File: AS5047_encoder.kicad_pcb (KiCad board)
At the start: 2 copper layers, 8 parts, among them P1 CONN_01X07, U1 AS5047

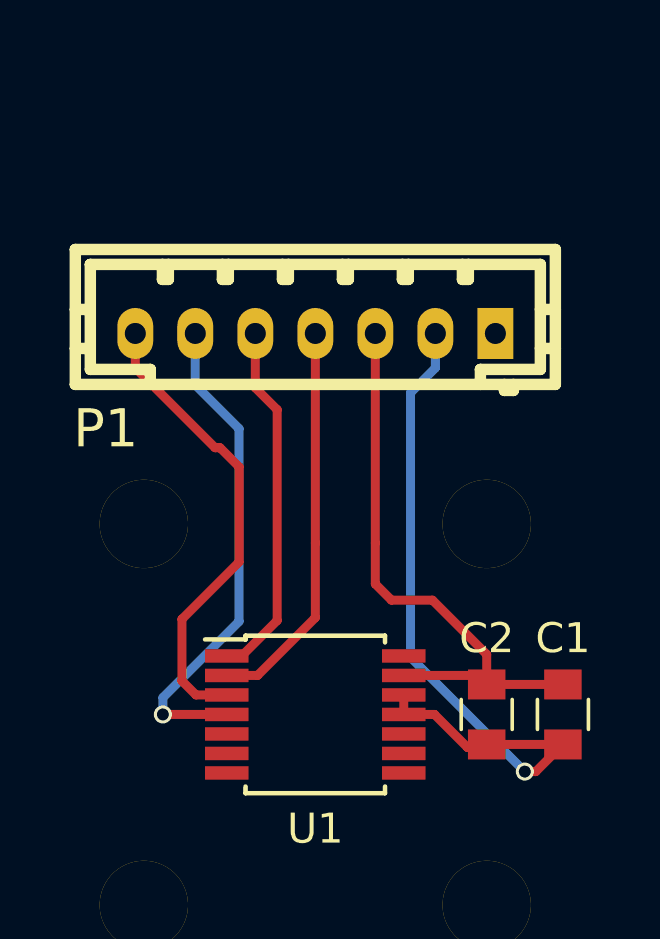
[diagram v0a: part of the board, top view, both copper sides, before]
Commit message: Change connector and update component associations.
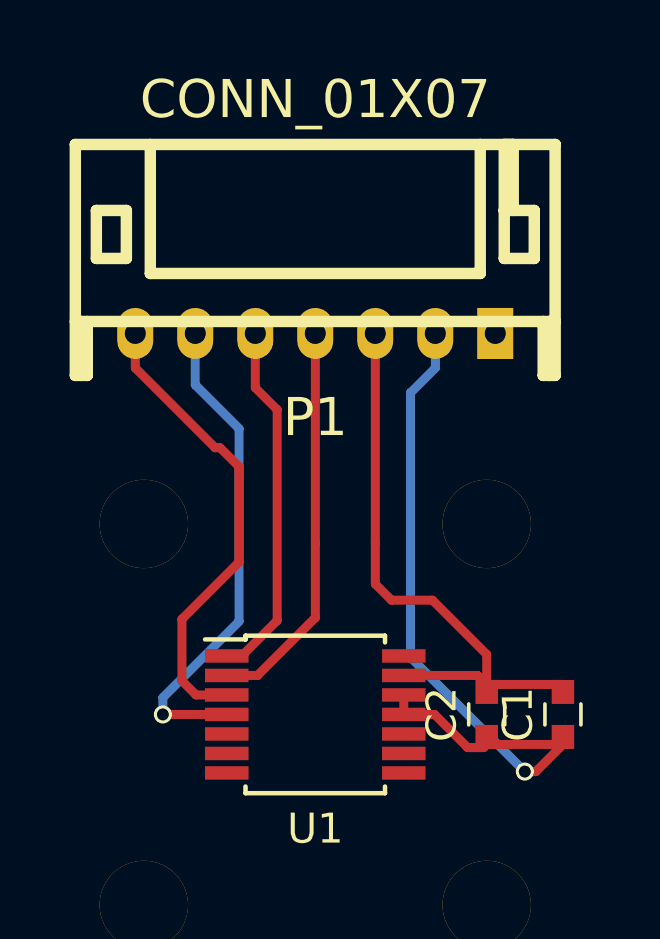
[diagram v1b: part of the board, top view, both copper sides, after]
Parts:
- C1, C2: footprint Capacitors_SMD:C_0805 -> Capacitors_SMD:C_0603
- P1: footprint w_conn_jst-ph:b7b-ph-kl -> w_conn_jst-ph:s7b-ph-kl

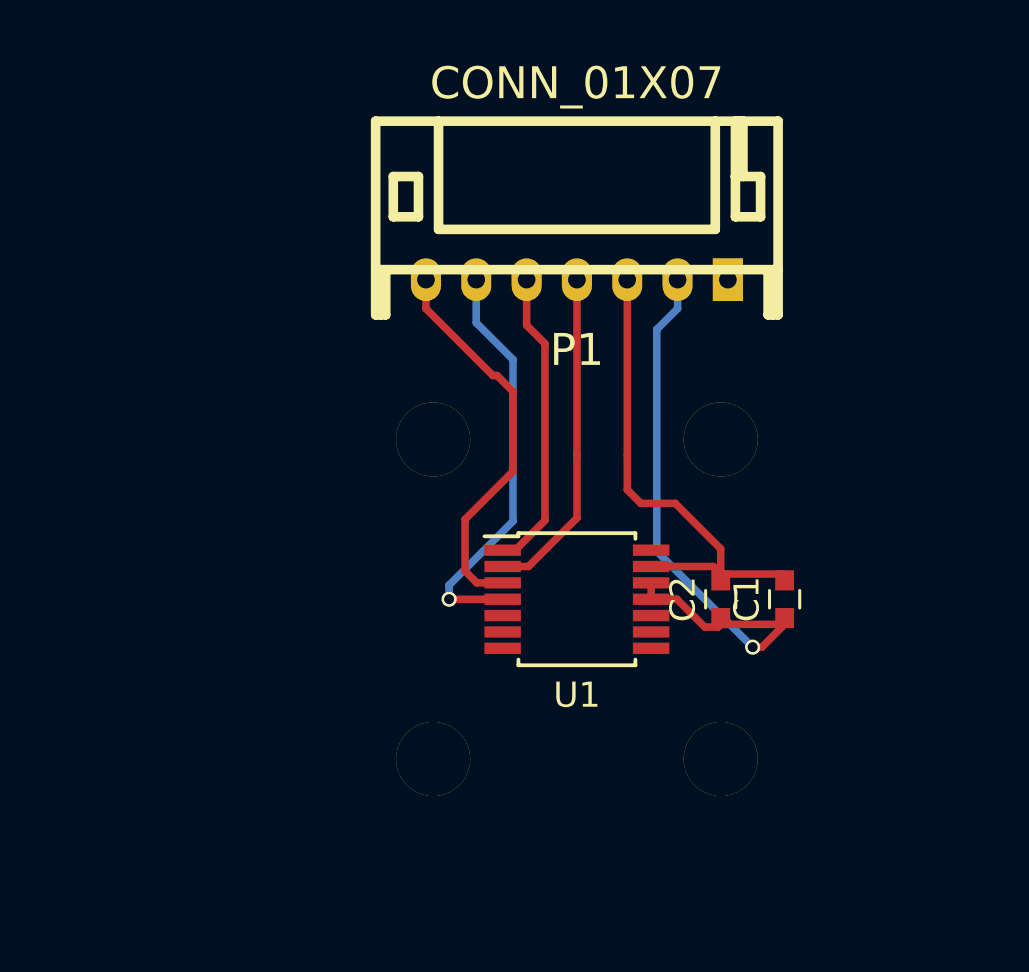
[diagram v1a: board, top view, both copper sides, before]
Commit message: Fixed outline. Generated gerbers. Added BOM. Ordered a batch of boards.
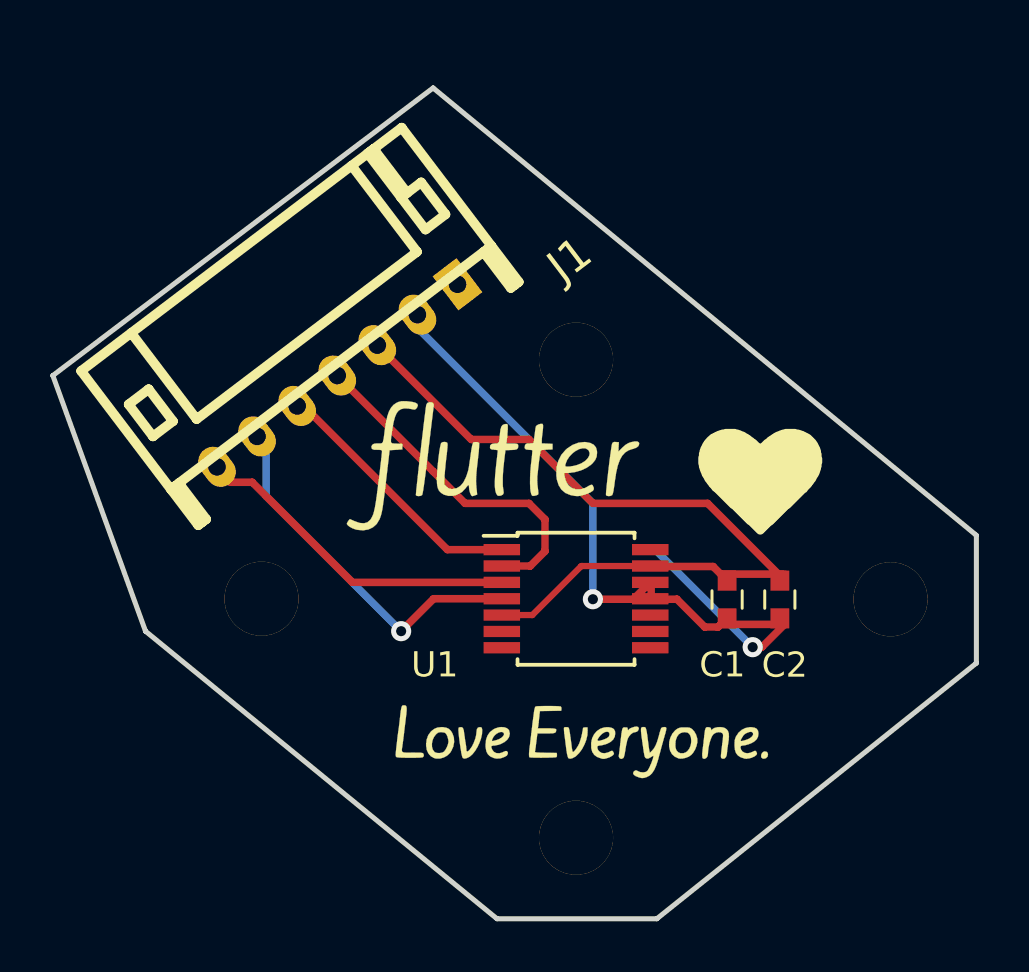
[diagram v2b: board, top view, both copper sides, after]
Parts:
- added G***: LOGO, vesc_encoder:love_small, F.Cu at (89.8, 102.1)
- added G***: LOGO, vesc_encoder:flutter_small, F.Cu at (86.5, 91.2)
- moved REF** 13.7 mm to (88.9, 102.9)
- moved J1 10.3 mm to (80.0, 87.6), turned to 217.2 degrees
- moved REF** 9.92 mm to (102.9, 96.5)
- moved REF** 8.98 mm to (77.5, 96.5)
- moved REF** 6.35 mm to (88.9, 90.2)
- moved C2 2.35 mm to (97.6, 96.5)
- moved C1 2.29 mm to (95.5, 96.5)
- renumbered P1 to J1
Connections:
- net Net-(C1-Pad1) renamed /VCC
- net Net-(P1-Pad4) renamed /CLK
- net Net-(P1-Pad5) renamed /CSn
- net Net-(P1-Pad6) renamed /MOSI
- net Net-(P1-Pad7) renamed /MISO
- U1 pad 5: Net-(U1-Pad5) -> GND
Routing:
- net GND: track 19.5 -> 32.1 mm
- net /VCC: track 24.6 -> 30.7 mm, vias 1 -> 2
- net /MISO: track 15.6 -> 13.5 mm
- net /MOSI: track 16.5 -> 14.8 mm
- net /CSn: track 12.0 -> 10.7 mm
- net /CLK: track 13.2 -> 13.9 mm
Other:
- board outline added: 36.7 x 33 mm
- net class Default: clearance 0.2 -> 0.1524; trace_width 0.3 -> 0.25
- rule trace_clearance: 0.2 -> 0.1524

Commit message: Imported to a new Kicad install and removed remnant traces from PCB layout. Suggest re-export gerbers to remove benign extra trace.
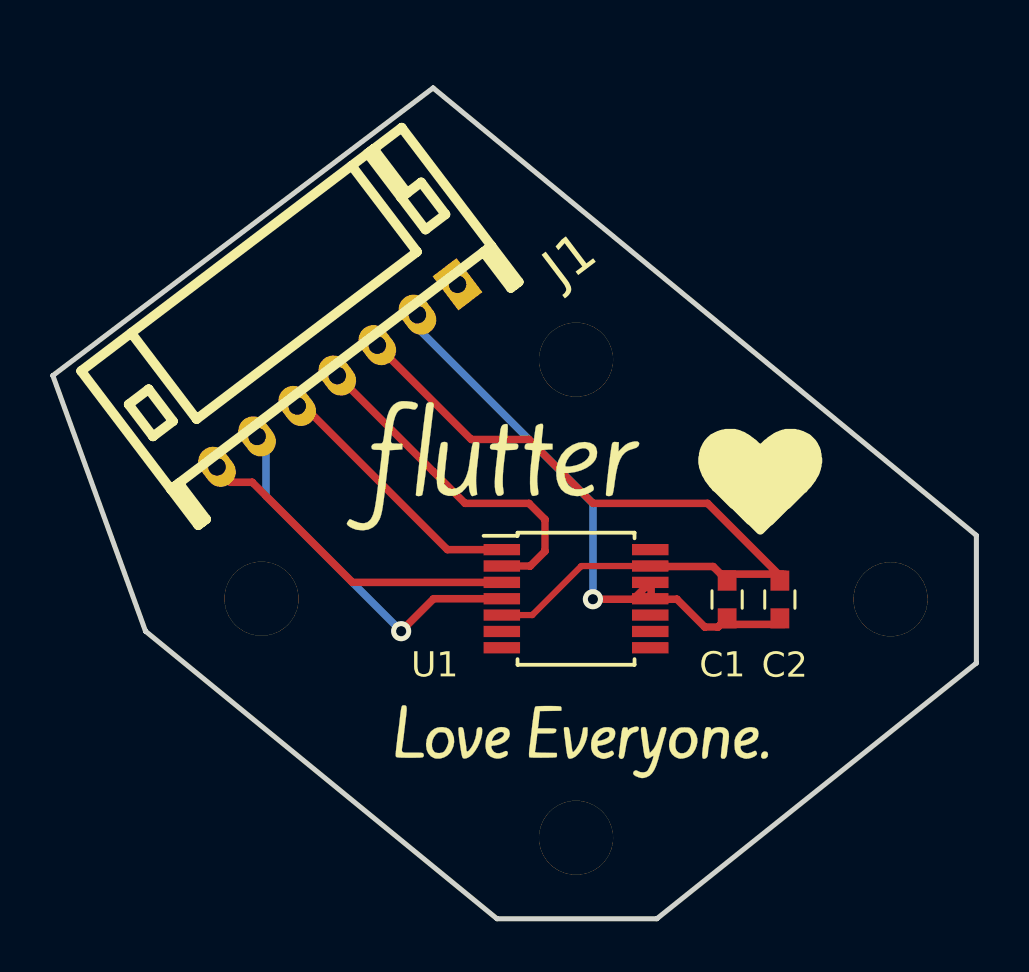
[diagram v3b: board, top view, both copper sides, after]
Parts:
- ? (x4): renamed from REF**; value VAL** -> (none)
- ? (x2): renamed from G***; value LOGO -> (none)
- C1, C2: value C -> (none)
- J1: value CONN_01X07 -> (none)
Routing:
- net /VCC: track 30.7 -> 23.6 mm, vias 2 -> 1
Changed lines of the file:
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@@
-(kicad_pcb (version 4) (host pcbnew 4.0.7+dfsg1-1)
+(kicad_pcb (version 20171130) (host pcbnew 5.0.2+dfsg1-1)
   (general
-    (links 0)
-    (no_connects 0)
-    (area 67.030233 75.194993 105.510001 109.320001)
     (thickness 1.6)
-    (drawings 9)
-    (tracks 52)
+    (drawings 11)
+    (tracks 48)
     (zones 0)
     (modules 10)
@@
     (36 B.SilkS user)
     (37 F.SilkS user)
-    (38 B.Mask user)
+    (38 B.Mask user hide)
     (39 F.Mask user)
-    (40 Dwgs.User user hide)
-    (41 Cmts.User user hide)
+    (40 Dwgs.User user)
+    (41 Cmts.User user)
     (42 Eco1.User user hide)
     (43 Eco2.User user hide)
@@
     (47 F.CrtYd user hide)
     (48 B.Fab user hide)
-    (49 F.Fab user hide)
+    (49 F.Fab user)
   )
   (setup
@@
     (pad_drill 0.762)
     (pad_to_mask_clearance 0.2)
+    (solder_mask_min_width 0.25)
     (aux_axis_origin 0 0)
-    (visible_elements FFFD5FBF)
+    (visible_elements FFFFDFFF)
     (pcbplotparams
       (layerselection 0x010fc_80000001)
       (usegerberextensions true)
+      (usegerberattributes false)
+      (usegerberadvancedattributes false)
+      (creategerberjobfile false)
       (excludeedgelayer true)
       (linewidth 0.100000)
@@
       (hpglpennumber 1)
       (hpglpenspeed 20)
-      (hpglpendiameter 15)
-      (hpglpenoverlay 2)
+      (hpglpendiameter 15.000000)
       (psnegative false)
       (psa4output false)
@@
       (drillshape 0)
       (scaleselection 1)
-      (outputdirectory Gerber))
+      (outputdirectory "Gerber"))
   )
   (net 0 "")
@@
     (descr "JST PH series connector, S7B-PH-KL")
     (fp_text reference J1 (at -10.138672 -1.905389 217.2) (layer F.SilkS)
-      (effects (font (thickness 0.3048)))
-    )
-    (fp_text value CONN_01X07 (at 0.810465 9.225022 217.2) (layer F.SilkS) hide
-      (effects (font (thickness 0.3048)))
+      (effects (font (size 1.524 1.524) (thickness 0.3048)))
+    )
+    (fp_text value "" (at 0.810465 9.225022 217.2) (layer F.SilkS) hide
+      (effects (font (size 1.524 1.524) (thickness 0.3048)))
     )
     (fp_line (start -6.2992 4.09956) (end -6.2992 6.2992) (layer F.SilkS) (width 0.381))
@@
     (pad 2 thru_hole oval (at -4.0005 0 217.2) (size 1.19888 1.69926) (drill 0.70104) (layers *.Cu *.Mask F.SilkS)
       (net 8 /VCC))
-    (pad 3 thru_hole oval (at -1.99898 0 217.2) (size 1.19888 1.69926) (drill 0.70104) (layers *.Cu *.Mask F.SilkS)
+    (pad 3 thru_hole oval (at -1.99898 0.000001 217.2) (size 1.19888 1.69926) (drill 0.70104) (layers *.Cu *.Mask F.SilkS)
       (net 6 GND))
     (pad 4 thru_hole oval (at 0 0 217.2) (size 1.19888 1.69926) (drill 0.70104) (layers *.Cu *.Mask F.SilkS)
       (net 9 /CLK))
-    (pad 5 thru_hole oval (at 1.99898 0 217.2) (size 1.19888 1.69926) (drill 0.70104) (layers *.Cu *.Mask F.SilkS)
+    (pad 5 thru_hole oval (at 1.99898 -0.000001 217.2) (size 1.19888 1.69926) (drill 0.70104) (layers *.Cu *.Mask F.SilkS)
       (net 10 /CSn))
     (pad 6 thru_hole oval (at 4.0005 0 217.2) (size 1.19888 1.69926) (drill 0.70104) (layers *.Cu *.Mask F.SilkS)
@@
     (descr "Mounting Hole - Screw #4")
     (attr virtual)
-    (fp_text reference REF** (at 0 -4.6) (layer F.SilkS) hide
+    (fp_text reference "" (at 0 -2.54) (layer F.SilkS) hide
       (effects (font (size 1 1) (thickness 0.18)))
     )
-    (fp_text value VAL** (at 0 4.7) (layer F.Fab) hide
+    (fp_text value "" (at 0 4.7) (layer F.Fab) hide
       (effects (font (size 1 1) (thickness 0.18)))
     )
@@
     (descr "Mounting Hole - Screw #4")
     (attr virtual)
-    (fp_text reference REF** (at 0 -4.6) (layer F.SilkS) hide
+    (fp_text reference "" (at 0 -4.6) (layer F.SilkS) hide
       (effects (font (size 1 1) (thickness 0.18)))
     )
-    (fp_text value VAL** (at 0 4.7) (layer F.Fab) hide
+    (fp_text value "" (at 0 4.7) (layer F.Fab) hide
       (effects (font (size 1 1) (thickness 0.18)))
     )
@@
     (descr "Mounting Hole - Screw #4")
     (attr virtual)
-    (fp_text reference REF** (at 0 -4.6) (layer F.SilkS) hide
+    (fp_text reference "" (at 0 -4.6) (layer F.SilkS) hide
       (effects (font (size 1 1) (thickness 0.18)))
     )
-    (fp_text value VAL** (at 0 4.7) (layer F.Fab) hide
+    (fp_text value "" (at 0 4.7) (layer F.Fab) hide
       (effects (font (size 1 1) (thickness 0.18)))
     )
@@
     (descr "Mounting Hole - Screw #4")
     (attr virtual)
-    (fp_text reference REF** (at 0 -4.6) (layer F.SilkS) hide
+    (fp_text reference "" (at 0 -4.6) (layer F.SilkS) hide
       (effects (font (size 1 1) (thickness 0.18)))
     )
-    (fp_text value VAL** (at 0 4.7) (layer F.Fab) hide
+    (fp_text value "" (at 0 4.7) (layer F.Fab) hide
       (effects (font (size 1 1) (thickness 0.18)))
     )
@@
       (effects (font (size 1 1) (thickness 0.15)))
     )
-    (fp_text value C (at 0 1.5 90) (layer F.Fab)
+    (fp_text value "" (at 0 1.5 90) (layer F.Fab) hide
       (effects (font (size 1 1) (thickness 0.15)))
     )
@@
       (effects (font (size 1 1) (thickness 0.15)))
     )
-    (fp_text value C (at 0 1.5 90) (layer F.Fab)
+    (fp_text value "" (at 0 1.5 90) (layer F.Fab)
       (effects (font (size 1 1) (thickness 0.15)))
     )
@@
   (module vesc_encoder:love_small (layer Top)
     (at 89.789 102.108)
-    (fp_text reference G*** (at 0 0) (layer F.SilkS) hide
-      (effects (font (thickness 0.3)))
-    )
-    (fp_text value LOGO (at 0.75 0) (layer F.SilkS) hide
-      (effects (font (thickness 0.3)))
+    (fp_text reference "" (at 15.621 5.842) (layer F.SilkS) hide
+      (effects (font (size 1.524 1.524) (thickness 0.3)))
+    )
+    (fp_text value "" (at 0.75 0) (layer F.SilkS) hide
+      (effects (font (size 1.524 1.524) (thickness 0.3)))
     )
     (fp_poly (pts (xy 2.41751 -0.507735) (xy 2.444613 -0.503325) (xy 2.466564 -0.489352) (xy 2.484926 -0.460398)
@@
   (module vesc_encoder:flutter_small (layer Top)
     (at 86.487 91.186)
-    (fp_text reference G*** (at 0 0) (layer F.SilkS) hide
-      (effects (font (thickness 0.3)))
-    )
-    (fp_text value LOGO (at 0.75 0) (layer F.SilkS) hide
-      (effects (font (thickness 0.3)))
+    (fp_text reference "" (at 0 0) (layer F.SilkS) hide
+      (effects (font (size 1.524 1.524) (thickness 0.3)))
+    )
+    (fp_text value "" (at 0.75 0) (layer F.SilkS) hide
+      (effects (font (size 1.524 1.524) (thickness 0.3)))
     )
     (fp_poly (pts (xy -3.708083 -2.532209) (xy -3.703806 -2.531935) (xy -3.506396 -2.510907) (xy -3.369681 -2.476387)
@@
       (xy 5.349031 -0.939972) (xy 5.456091 -0.935027)) (layer F.SilkS) (width 0.01))
   )
+  (dimension 33.020977 (width 0.3) (layer Dwgs.User)
+    (gr_text "33.021 mm" (at 59.55082 92.52429 89.55927193) (layer Dwgs.User)
+      (effects (font (size 1.5 1.5) (thickness 0.3)))
+    )
+    (feature1 (pts (xy 83.566 109.22) (xy 58.07386 109.023906)))
+    (feature2 (pts (xy 83.82 76.2) (xy 58.32786 76.003906)))
+    (crossbar (pts (xy 61.02778 76.024675) (xy 60.77378 109.044675)))
+    (arrow1a (pts (xy 60.77378 109.044675) (xy 60.196042 107.913694)))
+    (arrow1b (pts (xy 60.77378 109.044675) (xy 61.368849 107.922715)))
+    (arrow2a (pts (xy 61.02778 76.024675) (xy 60.432711 77.146635)))
+    (arrow2b (pts (xy 61.02778 76.024675) (xy 61.605518 77.155656)))
+  )
+  (dimension 36.703 (width 0.3) (layer Dwgs.User)
+    (gr_text "36.703 mm" (at 86.9315 69.643) (layer Dwgs.User)
+      (effects (font (size 1.5 1.5) (thickness 0.3)))
+    )
+    (feature1 (pts (xy 105.283 87.63) (xy 105.283 68.293)))
+    (feature2 (pts (xy 68.58 87.63) (xy 68.58 68.293)))
+    (crossbar (pts (xy 68.58 70.993) (xy 105.283 70.993)))
+    (arrow1a (pts (xy 105.283 70.993) (xy 104.156496 71.579421)))
+    (arrow1b (pts (xy 105.283 70.993) (xy 104.156496 70.406579)))
+    (arrow2a (pts (xy 68.58 70.993) (xy 69.706504 71.579421)))
+    (arrow2b (pts (xy 68.58 70.993) (xy 69.706504 70.406579)))
+  )
   (gr_circle (center 77 96.5) (end 79.5 96.5) (layer Dwgs.User) (width 0.2))
   (gr_line (start 68.707 87.63) (end 83.82 76.2) (layer Edge.Cuts) (width 0.2))
@@
   (segment (start 90.17 92.71) (end 90.17 96.52) (width 0.3) (layer Bottom) (net 8))
   (segment (start 82.838781 84.801219) (end 82.838781 85.378781) (width 0.3) (layer Bottom) (net 8))
-  (segment (start 92.71 94.615) (end 96.52 98.425) (width 0.3) (layer Bottom) (net 8))
-  (segment (start 96.52 98.425) (end 96.885 98.425) (width 0.3) (layer Top) (net 8))
-  (segment (start 96.885 98.425) (end 97.79 97.52) (width 0.3) (layer Top) (net 8))
-  (via (at 96.52 98.425) (size 0.8) (drill 0.4) (layers Top Bottom) (net 8))
   (segment (start 95.25 97.52) (end 97.79 97.52) (width 0.3) (layer Top) (net 8))
   (segment (start 94.615 97.625) (end 95.145 97.625) (width 0.3) (layer Top) (net 8))
